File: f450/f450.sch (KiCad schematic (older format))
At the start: 13 parts, among them J1 Conn_01x02, U1 AP65111AWU, U2 ESP32-WROOM-32U

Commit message: WIP power section.
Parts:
- removed U2: ESP32-WROOM-32U, RF_Module:ESP32-WROOM-32U, symbol RF_Module:ESP32-WROOM-32U
- added C4, C5, C6, C7: 22u, symbol Device:C
- added J2, J3, J4, J5: Conn_01x02, symbol Connector_Generic:Conn_01x02
- added U2: TLV70033_SOT23-5, Package_TO_SOT_SMD:SOT-23-5, symbol Regulator_Linear:TLV70033_SOT23-5
- added U3: LD1117S33TR_SOT223, Package_TO_SOT_SMD:SOT-223-3_TabPin2, symbol Regulator_Linear:LD1117S33TR_SOT223
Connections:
- net GND: now also C4.2, C5.2, C6.2, C7.2, U2.2 (GND), U3.1 (GND)
- net GNDPWR: now also J2.1 (Pin_1), J3.1 (Pin_1), J4.1 (Pin_1), J5.1 (Pin_1)
- net V_BAT: now also J2.2 (Pin_2), J3.2 (Pin_2), J4.2 (Pin_2), J5.2 (Pin_2)
- net +5 renamed 5V
- net 5V: now also C4.1, C6.1, U2.1 (IN), U2.3 (EN), U3.3 (VI)
- new net 3V3_CPU: C7.1, U3.2 (VO)
- new net 3V3_SENSOR: C5.1, U2.5 (OUT)
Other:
- moved on the sheet: C1, C2, C3, D1, L1, R1, R2, R3, R4, R5, U1

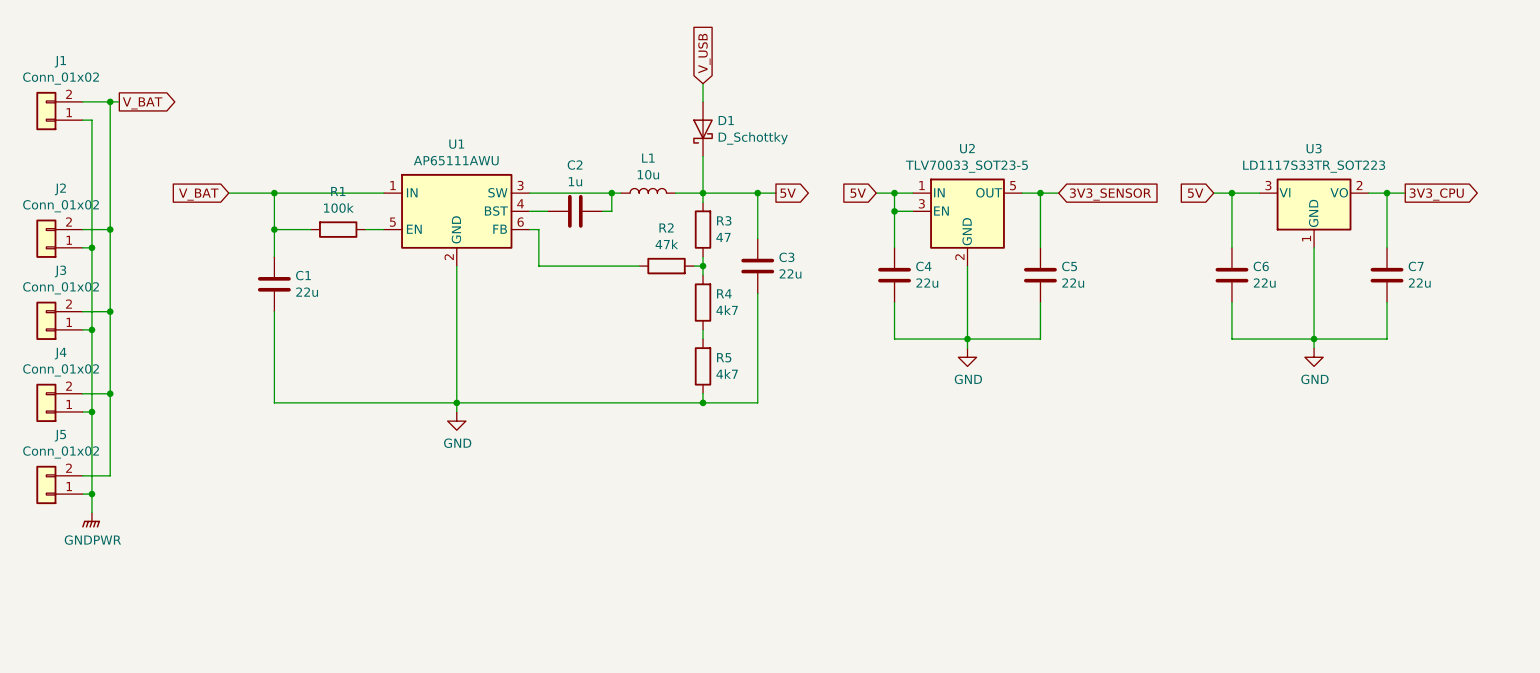
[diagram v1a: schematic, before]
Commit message: Added board CAD design. Schematic power section, USB-UART converter.
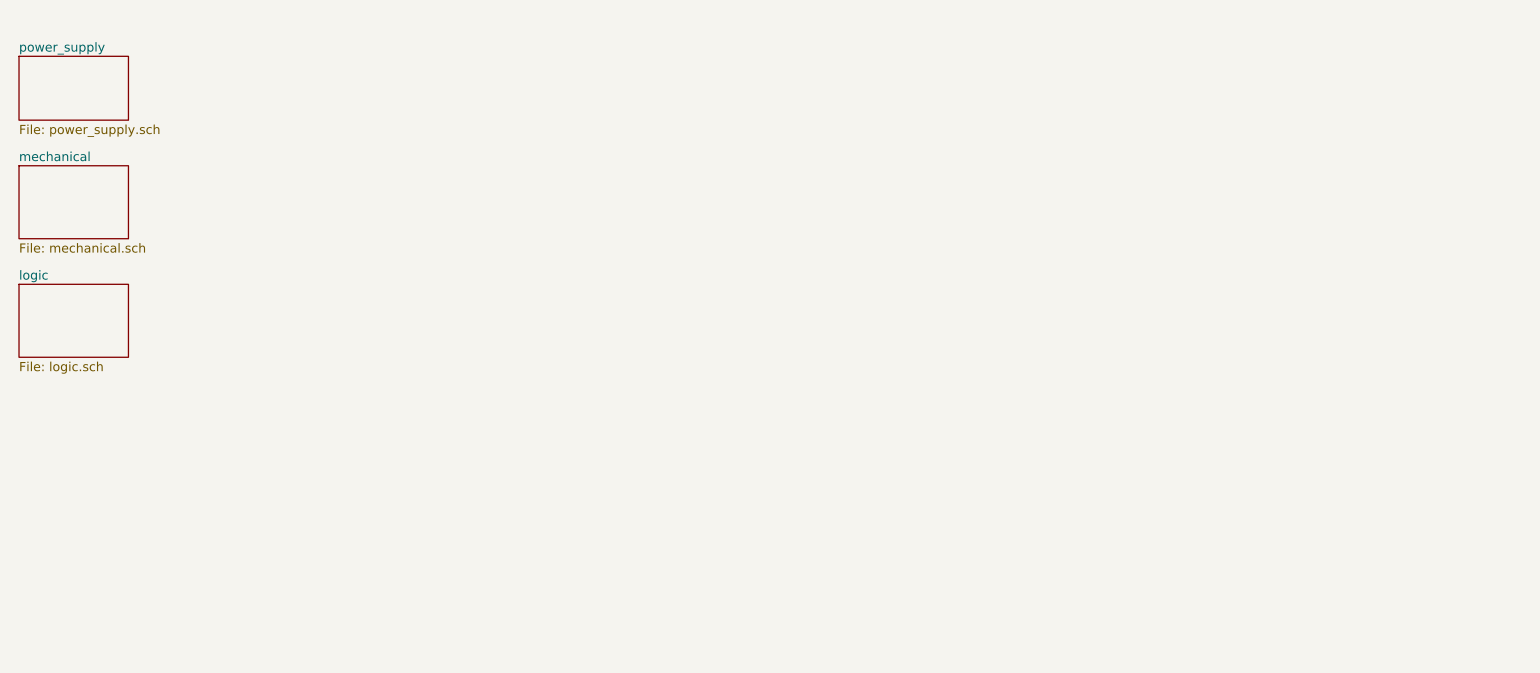
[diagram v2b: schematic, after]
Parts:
- removed C1, C3, C4, C5, C6, C7: 22u, symbol Device:C
- removed C2: 1u, symbol Device:C
- removed D1: D_Schottky, symbol Device:D_Schottky
- removed J1, J2, J3, J4, J5: Conn_01x02, symbol Connector_Generic:Conn_01x02
- removed L1: 10u, symbol Device:L
- removed R1: 100k, symbol Device:R
- removed R2: 47k, symbol Device:R
- removed R3: 47, symbol Device:R
- removed R4, R5: 4k7, symbol Device:R
- removed U1: AP65111AWU, Package_TO_SOT_SMD:TSOT-23-6, symbol Regulator_Switching:AP65111AWU
- removed U2: TLV70033_SOT23-5, Package_TO_SOT_SMD:SOT-23-5, symbol Regulator_Linear:TLV70033_SOT23-5
- removed U3: LD1117S33TR_SOT223, Package_TO_SOT_SMD:SOT-223-3_TabPin2, symbol Regulator_Linear:LD1117S33TR_SOT223
